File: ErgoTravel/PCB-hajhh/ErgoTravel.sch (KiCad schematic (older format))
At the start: 70 parts, among them J1 , J10 AudioJack3_Ground, J11 AudioJack3_Ground, J2 , J3 , J4 , J5 , J6 , J7 , J8 , SW1 , SW10 , SW11 , SW12 , SW13 , SW14 , SW15 , SW16 , SW17 , SW18 , SW19 , SW2 , SW20 , SW21 , SW22 , SW23 , SW24 , SW25 , SW26 , SW27 , SW28 , SW29 RST, SW3 , SW30 , SW31 , SW4 , SW5 , SW6 , SW7 , SW8 , SW9 , U1 Promicro

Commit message: update 13:33 24/01/2021
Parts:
- removed J10, J11: AudioJack3_Ground, Connector_Audio:Jack_3.5mm_PJ320D_Horizontal, symbol Connector:AudioJack3_Ground
- added D28: (no value), fruitkt:DIODE, symbol Device:D
- added J11, J15: (no value), Connector_PinHeader_2.54mm:PinHeader_1x02_P2.54mm_Vertical, symbol Connector_Generic:Conn_01x02
- added J12: OLED, fruitkt:OLED-0.91, symbol Connector_Generic:Conn_01x04
- added J13, J14: (no value), fruitkt:USB-C-16pin-hight, symbol Connector:USB_C_Receptacle_USB2.0
- added J16: AVR-ISP-6, Connector_PinHeader_2.54mm:PinHeader_2x03_P2.54mm_Vertical, symbol Connector:AVR-ISP-6
- added J3, J4: AudioJack4, Connector_Audio:Jack_3.5mm_PJ320D_Horizontal, symbol Connector:AudioJack4
- added JP1, JP2, JP3, JP4, JP5, JP6, JP7, JP8: (no value), footprints:Jump, symbol Device:Jumper_NC_Small
- added JP10, JP9: (no value), Jumper:SolderJumper-3_P1.3mm_Bridged12_Pad1.0x1.5mm_NumberLabels, symbol Jumper:SolderJumper_3_Bridged12
- added LED1, LED15, LED16, LED17, LED18, LED19, LED2, LED20, LED23, LED3, LED4, LED5, LED6, LED7: (no value), footprints:SK6812mini-e-R2L, symbol fruitkt:6812
- added LED10, LED11, LED12, LED13, LED14, LED21, LED22, LED24, LED25, LED26, LED27, LED8, LED9: (no value), footprints:SK6812mini-e-L2R, symbol fruitkt:6812
- added LED28, LED29, LED30, LED31, LED32, LED33: (no value), fruitkt:SK6812MINI-FLIP, symbol fruitkt:6812
- added R1, R2: 4K7, Resistor_SMD:R_0805_2012Metric, symbol Device:R_Small
- D1, D10, D19: footprint (none) -> fruitkt:DIODE
- D11: renamed from D14; footprint (none) -> fruitkt:DIODE
- D12: renamed from D18; footprint (none) -> fruitkt:DIODE
- D13: renamed from D22; footprint (none) -> fruitkt:DIODE
- D14: renamed from D26; footprint (none) -> fruitkt:DIODE
- D15: renamed from D3; footprint (none) -> fruitkt:DIODE
- D16: renamed from D7; footprint (none) -> fruitkt:DIODE
- D17: renamed from D11; footprint (none) -> fruitkt:DIODE
- D18: renamed from D15; footprint (none) -> fruitkt:DIODE
- D2: renamed from D5; footprint (none) -> fruitkt:DIODE
- D20: renamed from D23; footprint (none) -> fruitkt:DIODE
- D21: renamed from D27; footprint (none) -> fruitkt:DIODE
- D22: renamed from D4; footprint (none) -> fruitkt:DIODE
- D23: renamed from D8; footprint (none) -> fruitkt:DIODE
- D24: renamed from D12; footprint (none) -> fruitkt:DIODE
- D25: renamed from D16; footprint (none) -> fruitkt:DIODE
- D26: renamed from D20; footprint (none) -> fruitkt:DIODE
- D27: renamed from D24; footprint (none) -> fruitkt:DIODE
- D3: renamed from D9; footprint (none) -> fruitkt:DIODE
- D4: renamed from D13; footprint (none) -> fruitkt:DIODE
- D5: renamed from D17; footprint (none) -> fruitkt:DIODE
- D6: renamed from D21; footprint (none) -> fruitkt:DIODE
- D7: renamed from D25; footprint (none) -> fruitkt:DIODE
- D8: renamed from D2; footprint (none) -> fruitkt:DIODE
- D9: renamed from D6; footprint (none) -> fruitkt:DIODE
- SW16: renamed from SW29; footprint Button_Switch_SMD:SW_SPST_TL3342 -> footprints:SW_TACT_ALPS_SKQGABE010
- SW8: renamed from SW30; footprint Button_Switch_SMD:SW_SPDT_PCM12 -> footprints:SW_SPDT_PCM12
- renumbered J8 to J10, J5 to J2, J2 to J5, J3 to J7, J7 to J8, J4 to J9, SW6 to SW10, SW10 to SW11, SW14 to SW12, SW18 to SW13, SW22 to SW14, SW27 to SW15, SW25 to SW17, SW31 to SW18, SW3 to SW19, SW5 to SW2, SW7 to SW20, SW11 to SW21, SW15 to SW22, SW19 to SW23, SW23 to SW24, SW28 to SW25, SW4 to SW26, SW8 to SW27, SW12 to SW28, SW16 to SW29, SW9 to SW3, SW20 to SW30, SW24 to SW31, SW13 to SW4, SW17 to SW5, SW21 to SW6, SW26 to SW7, SW2 to SW9
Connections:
- net GND: now also J11.2 (Pin_2), J13.A1 (GND), J13.A12 (GND), J13.B1 (GND), J13.B12 (GND), J13.S1 (SHIELD), J14.A1 (GND), J14.A12 (GND), J14.B1 (GND), J14.B12 (GND), J14.S1 (SHIELD), J16.6 (GND), J3.R2, J4.R2, JP4.1, JP5.1, LED1.-, LED10.-, LED11.-, LED12.-, LED13.-, LED14.-, LED15.-, LED16.-, LED17.-, LED18.-, LED19.-, LED2.-, LED20.-, LED21.-, LED22.-, LED23.-, LED24.-, LED25.-, LED26.-, LED27.-, LED28.-, LED29.-, LED3.-, LED30.-, LED31.-, LED32.-, LED33.-, LED4.-, LED5.-, LED6.-, LED7.-, LED8.-, LED9.-
- net col3: now reaches U1.B1 ((SCK)B1)
- net col3: now also SW12.1, SW22.1, SW29.1, SW4.1, J16.3 (SCK)
- net col5: now reaches U1.B2 ((MOSI)B2)
- net col5: now also SW14.1, SW24.1, SW31.1, SW6.1, J16.4 (MOSI)
- net col4: now reaches U1.B3 ((MISO)B3)
- net col4: now also SW13.1, SW23.1, SW30.1, SW5.1, J16.1 (MISO)
- net row3: now reaches U1.B4
- net row3: now also D22.1 (K), D23.1 (K), D24.1 (K), D25.1 (K), D26.1 (K), D27.1 (K), D28.1 (K)
- net backlight: now reaches U1.B5
- net col6: now reaches U1.B6
- net col6: now also SW15.1, SW17.1, SW18.S1, SW25.2, SW7.1, J15.1 (Pin_1)
- net row0: now reaches U1.C6
- net row0: now also D1.1 (K), D2.1 (K), D3.1 (K), D4.1 (K), D5.1 (K), D6.1 (K), D7.1 (K)
- net scl: now reaches U1.D0 (D0(SCL))
- net scl: now also JP10.3 (B), JP2.1, JP7.1, R1.2
- net sda: now reaches U1.D1 (D1(SDA))
- net sda: now also JP1.1, JP8.1, JP9.3 (B), R2.2
- net rx: now reaches U1.D2 (D2(RX))
- net rx: now also JP10.1 (A), JP9.1 (A)
- net led: now reaches U1.D3 (D3(TX))
- net led: now also LED33.I (IN)
- net A: now reaches U1.D4
- net A: now also SW18.A
- net row1: now reaches U1.D7
- net row1: now also D10.1 (K), D11.1 (K), D12.1 (K), D13.1 (K), D14.1 (K), D8.1 (K), D9.1 (K)
- net row2: now reaches U1.E6
- net row2: now also D15.1 (K), D16.1 (K), D17.1 (K), D18.1 (K), D19.1 (K), D20.1 (K), D21.1 (K)
- net B: now reaches U1.F4
- net B: now also SW18.B
- net col0: now reaches U1.F5
- net col0: now also SW1.1, SW19.1, SW26.1, SW9.1
- net col1: now reaches U1.F6
- net col1: now also SW10.1, SW2.1, SW20.1, SW27.1
- net col2: now reaches U1.F7
- net col2: now also SW11.1, SW21.1, SW28.1, SW3.1
- net RST: now reaches SW16.1, U1.RST
- net RST: now also J16.5 (~RST)
- net VCC: now reaches U1.VCC
- net VCC: now also J13.A4 (VBUS), J13.A9 (VBUS), J13.B4 (VBUS), J13.B9 (VBUS), J14.A4 (VBUS), J14.A9 (VBUS), J14.B4 (VBUS), J14.B9 (VBUS), J16.2 (VCC), J3.R1, J4.R1, JP3.1, JP6.1, LED1.+, LED10.+, LED11.+, LED12.+, LED13.+, LED14.+, LED15.+, LED16.+, LED17.+, LED18.+, LED19.+, LED2.+, LED20.+, LED21.+, LED22.+, LED23.+, LED24.+, LED25.+, LED26.+, LED27.+, LED28.+, LED29.+, LED3.+, LED30.+, LED31.+, LED32.+, LED33.+, LED4.+, LED5.+, LED6.+, LED7.+, LED8.+, LED9.+, R1.1, R2.1
- net at SW18.S2: now also D21.2 (A), SW17.2, SW25.1
- net at SW8.3 (C): now also J11.1 (Pin_1)
- new net: J12.1 (Pin_1), JP1.2, JP5.2
- new net: J12.2 (Pin_2), JP2.2, JP6.2
- new net: J12.3 (Pin_3), JP3.2, JP7.2
- new net: J12.4 (Pin_4), JP4.2, JP8.2
- new net: LED32.I (IN), LED33.O (OUT)
- new net: LED31.I (IN), LED32.O (OUT)
- new net: LED30.I (IN), LED31.O (OUT)
- new net: LED29.I (IN), LED30.O (OUT)
- new net: LED28.I (IN), LED29.O (OUT)
- new net: LED1.I (IN), LED28.O (OUT)
- new net: J13.A5 (CC1), J14.A5 (CC1)
- new net: J13.A8 (SBU1), J14.A8 (SBU1)
- new net: J13.B5 (CC2), J14.B5 (CC2)
- new net: J13.B8 (SBU2), J14.B8 (SBU2)
- new net: LED1.O (OUT), LED2.I (IN)
- new net: LED2.O (OUT), LED3.I (IN)
- new net: LED3.O (OUT), LED4.I (IN)
- new net: LED4.O (OUT), LED5.I (IN)
- new net: LED5.O (OUT), LED6.I (IN)
- new net: LED6.O (OUT), LED7.I (IN)
- new net: LED14.I (IN), LED7.O (OUT)
- new net: LED13.I (IN), LED14.O (OUT)
- new net: LED12.I (IN), LED13.O (OUT)
- new net: LED11.I (IN), LED12.O (OUT)
- new net: LED10.I (IN), LED11.O (OUT)
- new net: LED10.O (OUT), LED9.I (IN)
- new net: LED8.I (IN), LED9.O (OUT)
- new net: LED15.I (IN), LED8.O (OUT)
- new net: LED15.O (OUT), LED16.I (IN)
- new net: LED16.O (OUT), LED17.I (IN)
- new net: LED17.O (OUT), LED18.I (IN)
- new net: LED18.O (OUT), LED19.I (IN)
- new net: LED19.O (OUT), LED20.I (IN)
- new net: LED20.O (OUT), LED21.I (IN)
- new net: LED21.O (OUT), LED27.I (IN)
- new net: LED26.I (IN), LED27.O (OUT)
- new net: LED25.I (IN), LED26.O (OUT)
- new net: LED24.I (IN), LED25.O (OUT)
- new net: LED22.I (IN), LED23.I (IN), LED24.O (OUT)
- new net: LED22.O (OUT), LED23.O (OUT)
- new net: D28.2 (A), J15.2 (Pin_2)
- new net 1: J13.A7 (D-), J13.B7 (D-), J14.A7 (D-), J14.B7 (D-), J3.S, J4.S, JP10.2 (C)
- new net 2: J13.A6 (D+), J13.B6 (D+), J14.A6 (D+), J14.B6 (D+), J3.T, J4.T, JP9.2 (C)
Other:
- moved on the sheet: D1, D10, D11, D12, D13, D14, D15, D16, D17, D18, D19, D2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

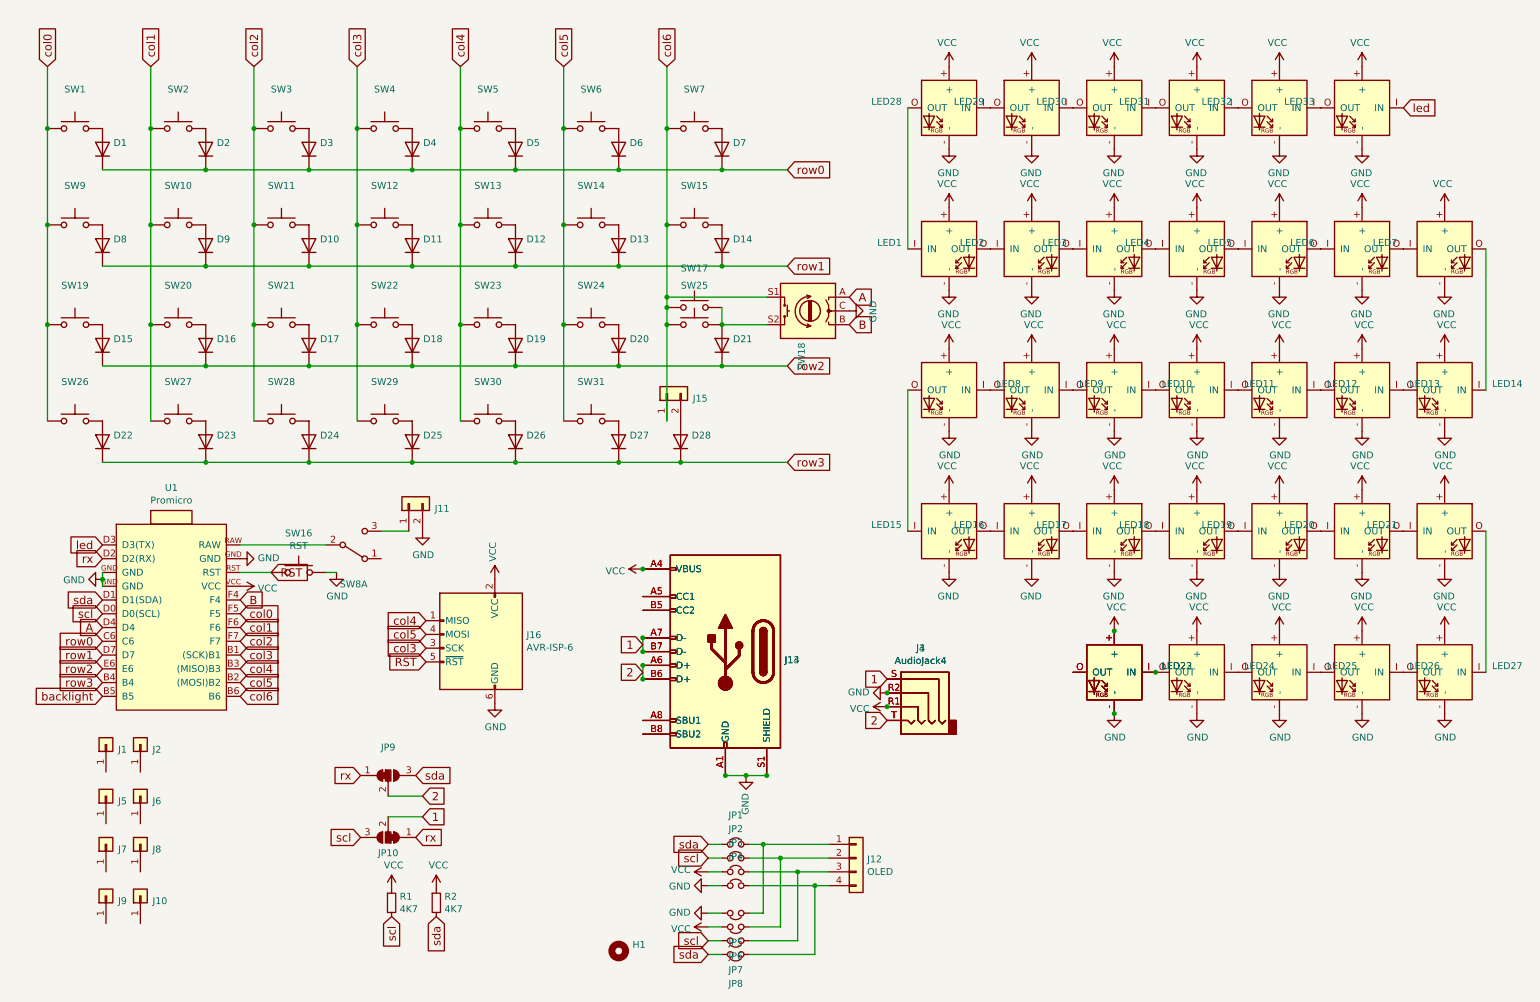
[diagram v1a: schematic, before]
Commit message: add some keyboard
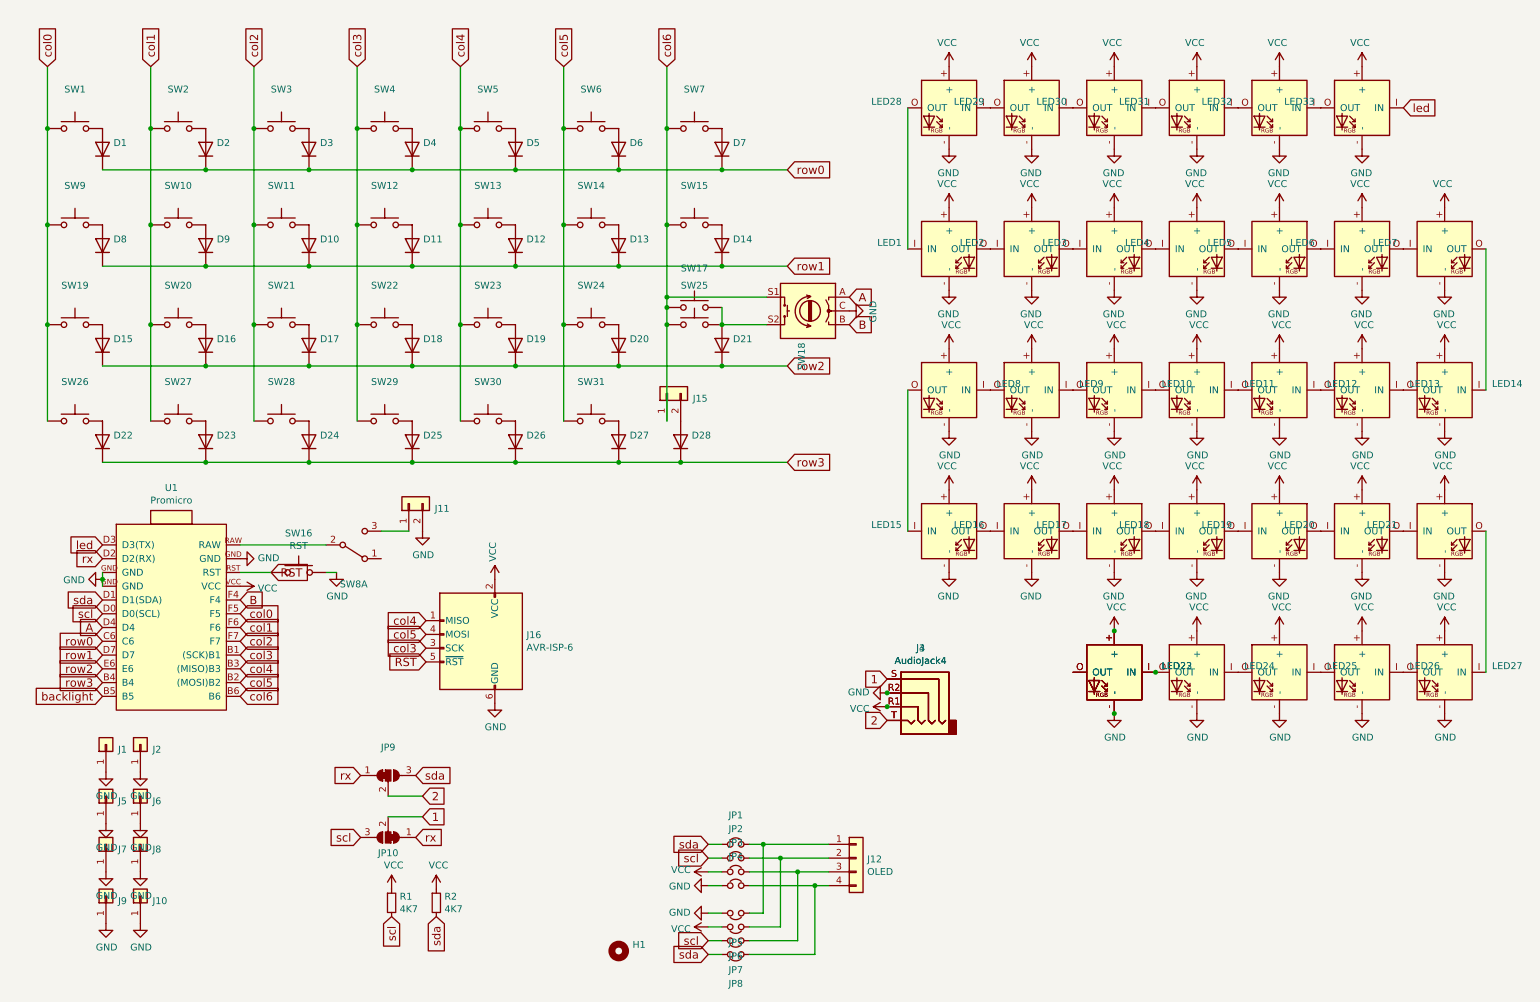
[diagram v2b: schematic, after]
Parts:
- removed J13, J14: (no value), fruitkt:USB-C-16pin-hight, symbol Connector:USB_C_Receptacle_USB2.0
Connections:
- net GND: now also J1.1 (Pin_1), J10.1 (Pin_1), J2.1 (Pin_1), J5.1 (Pin_1), J6.1 (Pin_1), J7.1 (Pin_1), J8.1 (Pin_1), J9.1 (Pin_1)
- net col3: now also SW4.2; no longer SW4.1
- net at D4.2 (A): now also SW4.1; no longer SW4.2
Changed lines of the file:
@@
 F 3 "~" H 3175 1650 50  0001 C CNN
 	1    3175 1450
-	1    0    0    -1
+	-1   0    0    -1
 $EndComp
 $Comp
@@
 Text GLabel 10575 1300 2    60   Input ~ 0
 led
-$Comp
-L Connector:USB_C_Receptacle_USB2.0 J13
-U 1 1 60161BE3
-P 5650 5250
-F 0 "J13" H 5220 5189 50  0000 R CNN
-F 1 " " H 5220 5098 50  0000 R CNN
-F 2 "fruitkt:USB-C-16pin-hight" H 5800 5250 50  0001 C CNN
-F 3 "https://www.usb.org/sites/default/files/documents/usb_type-c.zip" H 5800 5250 50  0001 C CNN
-	1    5650 5250
-	-1   0    0    -1
-$EndComp
 Connection ~ 6825 5550
 Connection ~ 6825 5650
-$Comp
-L power:GND #PWR0113
-U 1 1 60188703
-P 5800 6150
-F 0 "#PWR0113" H 5800 5900 50  0001 C CNN
-F 1 "GND" V 5805 6022 50  0000 R CNN
-F 2 "" H 5800 6150 50  0001 C CNN
-F 3 "" H 5800 6150 50  0001 C CNN
-	1    5800 6150
-	-1   0    0    -1
-$EndComp
-$Comp
-L power:VCC #PWR0114
-U 1 1 60188709
-P 5050 4650
-F 0 "#PWR0114" H 5050 4500 50  0001 C CNN
-F 1 "VCC" V 5065 4778 50  0000 L CNN
-F 2 "" H 5050 4650 50  0001 C CNN
-F 3 "" H 5050 4650 50  0001 C CNN
-	1    5050 4650
-	0    -1   1    0
-$EndComp
-Wire Wire Line
-	5650 6150 5800 6150
-Connection ~ 5800 6150
-Wire Wire Line
-	5800 6150 5950 6150
-$Comp
-L Connector:USB_C_Receptacle_USB2.0 J14
-U 1 1 60199990
-P 5650 5250
-F 0 "J14" H 5220 5189 50  0000 R CNN
-F 1 " " H 5220 5098 50  0000 R CNN
-F 2 "fruitkt:USB-C-16pin-hight" H 5800 5250 50  0001 C CNN
-F 3 "https://www.usb.org/sites/default/files/documents/usb_type-c.zip" H 5800 5250 50  0001 C CNN
-	1    5650 5250
-	-1   0    0    -1
-$EndComp
-Connection ~ 5050 4650
-Connection ~ 5650 6150
-Connection ~ 5950 6150
-Wire Wire Line
-	5050 5250 5050 5150
-Connection ~ 5050 5250
-Connection ~ 5050 5150
-Wire Wire Line
-	5050 5350 5050 5450
-Connection ~ 5050 5350
-Connection ~ 5050 5450
 Text GLabel 6825 5450 0    60   Input ~ 0
 1
 Text GLabel 6825 5750 0    60   Input ~ 0
-2
-Text GLabel 5050 5200 0    60   Input ~ 0
-1
-Text GLabel 5050 5400 0    60   Input ~ 0
 2
 $Comp
@@
 Text GLabel 3475 5325 0    60   Input ~ 0
 RST
+$Comp
+L power:GND #PWR0119
+U 1 1 60148C68
+P 1150 6125
+F 0 "#PWR0119" H 1150 5875 50  0001 C CNN
+F 1 "GND" H 1155 5952 50  0000 C CNN
+F 2 "" H 1150 6125 50  0001 C CNN
+F 3 "" H 1150 6125 50  0001 C CNN
+	1    1150 6125
+	1    0    0    -1
+$EndComp
+$Comp
+L power:GND #PWR0120
+U 1 1 601491C9
+P 1400 6125
+F 0 "#PWR0120" H 1400 5875 50  0001 C CNN
+F 1 "GND" H 1405 5952 50  0000 C CNN
+F 2 "" H 1400 6125 50  0001 C CNN
+F 3 "" H 1400 6125 50  0001 C CNN
+	1    1400 6125
+	1    0    0    -1
+$EndComp
+$Comp
+L power:GND #PWR0121
+U 1 1 6014E1A3
+P 1150 6500
+F 0 "#PWR0121" H 1150 6250 50  0001 C CNN
+F 1 "GND" H 1155 6327 50  0000 C CNN
+F 2 "" H 1150 6500 50  0001 C CNN
+F 3 "" H 1150 6500 50  0001 C CNN
+	1    1150 6500
+	1    0    0    -1
+$EndComp
+$Comp
+L power:GND #PWR0122
+U 1 1 6014E1A9
+P 1400 6500
+F 0 "#PWR0122" H 1400 6250 50  0001 C CNN
+F 1 "GND" H 1405 6327 50  0000 C CNN
+F 2 "" H 1400 6500 50  0001 C CNN
+F 3 "" H 1400 6500 50  0001 C CNN
+	1    1400 6500
+	1    0    0    -1
+$EndComp
+$Comp
+L power:GND #PWR0123
+U 1 1 60150D30
+P 1150 6850
+F 0 "#PWR0123" H 1150 6600 50  0001 C CNN
+F 1 "GND" H 1155 6677 50  0000 C CNN
+F 2 "" H 1150 6850 50  0001 C CNN
+F 3 "" H 1150 6850 50  0001 C CNN
+	1    1150 6850
+	1    0    0    -1
+$EndComp
+$Comp
+L power:GND #PWR0124
+U 1 1 60150D36
+P 1400 6850
+F 0 "#PWR0124" H 1400 6600 50  0001 C CNN
+F 1 "GND" H 1405 6677 50  0000 C CNN
+F 2 "" H 1400 6850 50  0001 C CNN
+F 3 "" H 1400 6850 50  0001 C CNN
+	1    1400 6850
+	1    0    0    -1
+$EndComp
+$Comp
+L power:GND #PWR0125
+U 1 1 6015389F
+P 1150 7225
+F 0 "#PWR0125" H 1150 6975 50  0001 C CNN
+F 1 "GND" H 1155 7052 50  0000 C CNN
+F 2 "" H 1150 7225 50  0001 C CNN
+F 3 "" H 1150 7225 50  0001 C CNN
+	1    1150 7225
+	1    0    0    -1
+$EndComp
+$Comp
+L power:GND #PWR0126
+U 1 1 601538A5
+P 1400 7225
+F 0 "#PWR0126" H 1400 6975 50  0001 C CNN
+F 1 "GND" H 1405 7052 50  0000 C CNN
+F 2 "" H 1400 7225 50  0001 C CNN
+F 3 "" H 1400 7225 50  0001 C CNN
+	1    1400 7225
+	1    0    0    -1
+$EndComp
 $EndSCHEMATC
